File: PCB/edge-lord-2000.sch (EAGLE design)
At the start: 40 parts, among them Q1 SI2302CDS, Q2 SI2302CDS, Q3 SI2302CDS, Q4 SI2302CDS, Q5 ON Semi NTS4173P, Q6 2N7002

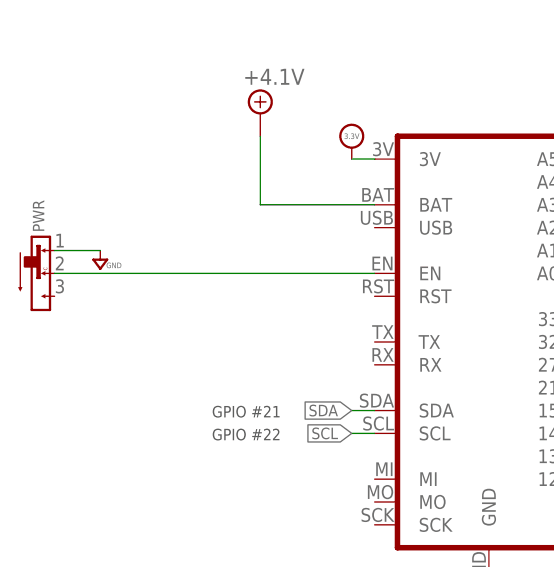
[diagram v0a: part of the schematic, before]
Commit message: PWR switch was backward. Updated 3D model for fusion.
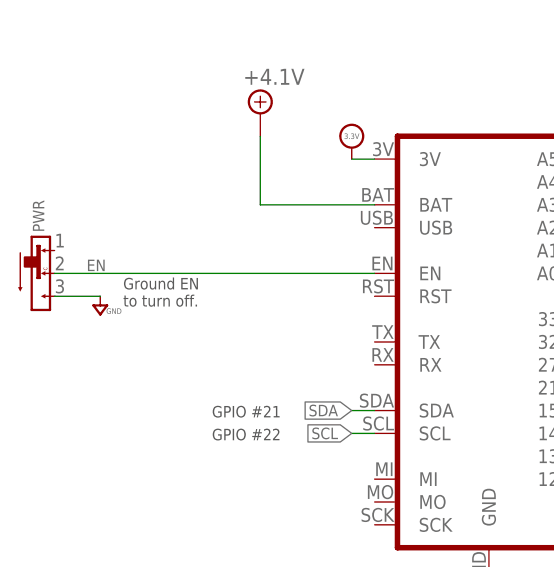
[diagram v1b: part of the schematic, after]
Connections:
- net N$1 renamed EN
- net GND: now also PWR.3; no longer PWR.1
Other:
- note added: "Ground EN to turn off."
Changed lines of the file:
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@@
 <text x="45.466" y="105.918" size="1.27" layer="97" align="bottom-right">GPIO #22</text>
 <text x="45.466" y="108.458" size="1.27" layer="97" align="bottom-right">GPIO #21</text>
+<text x="27.94" y="123.952" size="1.27" layer="97" align="top-left">Ground EN
+to turn off.</text>
 </plain>
 <instances>
@@
 </instance>
 <instance part="HUZZAH" gate="G$1" x="68.58" y="109.22" smashed="yes"/>
-<instance part="SUPPLY1" gate="GND" x="25.4" y="127" smashed="yes">
-<attribute name="VALUE" x="26.924" y="125.349" size="0.6096" layer="96" font="vector" align="center"/>
+<instance part="SUPPLY1" gate="GND" x="25.4" y="121.92" smashed="yes">
+<attribute name="VALUE" x="26.924" y="120.269" size="0.6096" layer="96" font="vector" align="center"/>
 </instance>
 <instance part="SUPPLY2" gate="GND" x="68.58" y="91.44" smashed="yes">
@@
 </busses>
 <nets>
-<net name="N$1" class="0">
+<net name="EN" class="0">
 <segment>
 <pinref part="HUZZAH" gate="G$1" pin="EN"/>
 <wire x1="55.88" y1="124.46" x2="20.32" y2="124.46" width="0.1524" layer="91"/>
 <pinref part="PWR" gate="G$1" pin="2"/>
+<label x="23.876" y="124.714" size="1.27" layer="95"/>
 </segment>
 </net>
@@
 <pinref part="HUZZAH" gate="G$1" pin="GND"/>
 <pinref part="SUPPLY2" gate="GND" pin="GND"/>
-</segment>
-<segment>
-<pinref part="SUPPLY1" gate="GND" pin="GND"/>
-<wire x1="20.32" y1="127" x2="25.4" y2="127" width="0.1524" layer="91"/>
-<pinref part="PWR" gate="G$1" pin="1"/>
 </segment>
 <segment>
@@
 <pinref part="SUPPLY35" gate="GND" pin="GND"/>
 </segment>
+<segment>
+<pinref part="PWR" gate="G$1" pin="3"/>
+<pinref part="SUPPLY1" gate="GND" pin="GND"/>
+<wire x1="20.32" y1="121.92" x2="25.4" y2="121.92" width="0.1524" layer="91"/>
+</segment>
 </net>

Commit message: PCB Rev.A tweaks.
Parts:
- R4: value XXX -> 330
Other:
- note added: "TODO: -nothing for now"
- note removed: "TODO: - P-FET needs 1N7002 on gate to work properly. - Caps accross motor load - Bulk cap for motor power. 47 -100uF - Power switch up/down reversed. - Measure motor draw when turned off. - Fuse on BAT out. - Fuse on sensor power. - Mode up/down buttons are swapped - Vibe connector TRS jack holes are enormous. Slim them down."

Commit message: Bodge Notes added to schematic
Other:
- note added: "Bodge Notes: - MOT2 and MOT3 don't work as they were routed onto INPUT only pins. Cut traces and moved to SCK(5) and MO (18) pins. But SCK has signal on it during programming. Causing motor to run. - Rev.B Move buttons to input only pins and use output pins (non-SCK) for motors."
- note added: "TODO: - change button pins to use input only pins. -change MOT3 MOT4 to use non-SCK/MO pins. - MOTORS connector channel order should be reversed, should go left to right."
- note removed: "TODO: -nothing for now"
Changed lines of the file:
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@@
 <text x="93.726" y="123.698" size="1.27" layer="97">GPIO #26</text>
 <text x="93.726" y="126.238" size="1.27" layer="97">GPIO #25</text>
-<text x="55.88" y="185.42" size="5.08" layer="97">TODO:
--nothing for now</text>
+<text x="7.62" y="53.34" size="2.54" layer="97">TODO:
+- change button pins to use input only pins.
+-change MOT3 MOT4 to use non-SCK/MO pins.
+- MOTORS connector channel order should
+  be reversed, should go left to right.</text>
 <text x="94.996" y="134.112" size="1.27" layer="97">GPIO #15</text>
 <text x="45.466" y="105.918" size="1.27" layer="97" align="bottom-right">GPIO #22</text>
@@
 <text x="27.94" y="123.952" size="1.27" layer="97" align="top-left">Ground EN
 to turn off.</text>
+<text x="5.08" y="17.78" size="2.54" layer="97">Bodge Notes:
+ - MOT2 and  MOT3 don't work as they were routed
+    onto INPUT only pins.  Cut traces and moved to
+    SCK(5) and MO (18) pins.  But SCK has signal on it during programming. Causing motor to run.
+ - Rev.B Move buttons to input only pins and use output pins (non-SCK) for motors.</text>
 </plain>
 <instances>
 <instance part="FRAME1" gate="G$1" x="0" y="0" smashed="yes">
-<attribute name="DOCUMENT_NUMBER" x="0" y="0" size="1.27" layer="96"/>
+<attribute name="DOCUMENT_NUMBER" x="10.16" y="5.08" size="1.27" layer="96" display="off"/>
 </instance>
 <instance part="FRAME1" gate="G$2" x="147.32" y="0" smashed="yes">

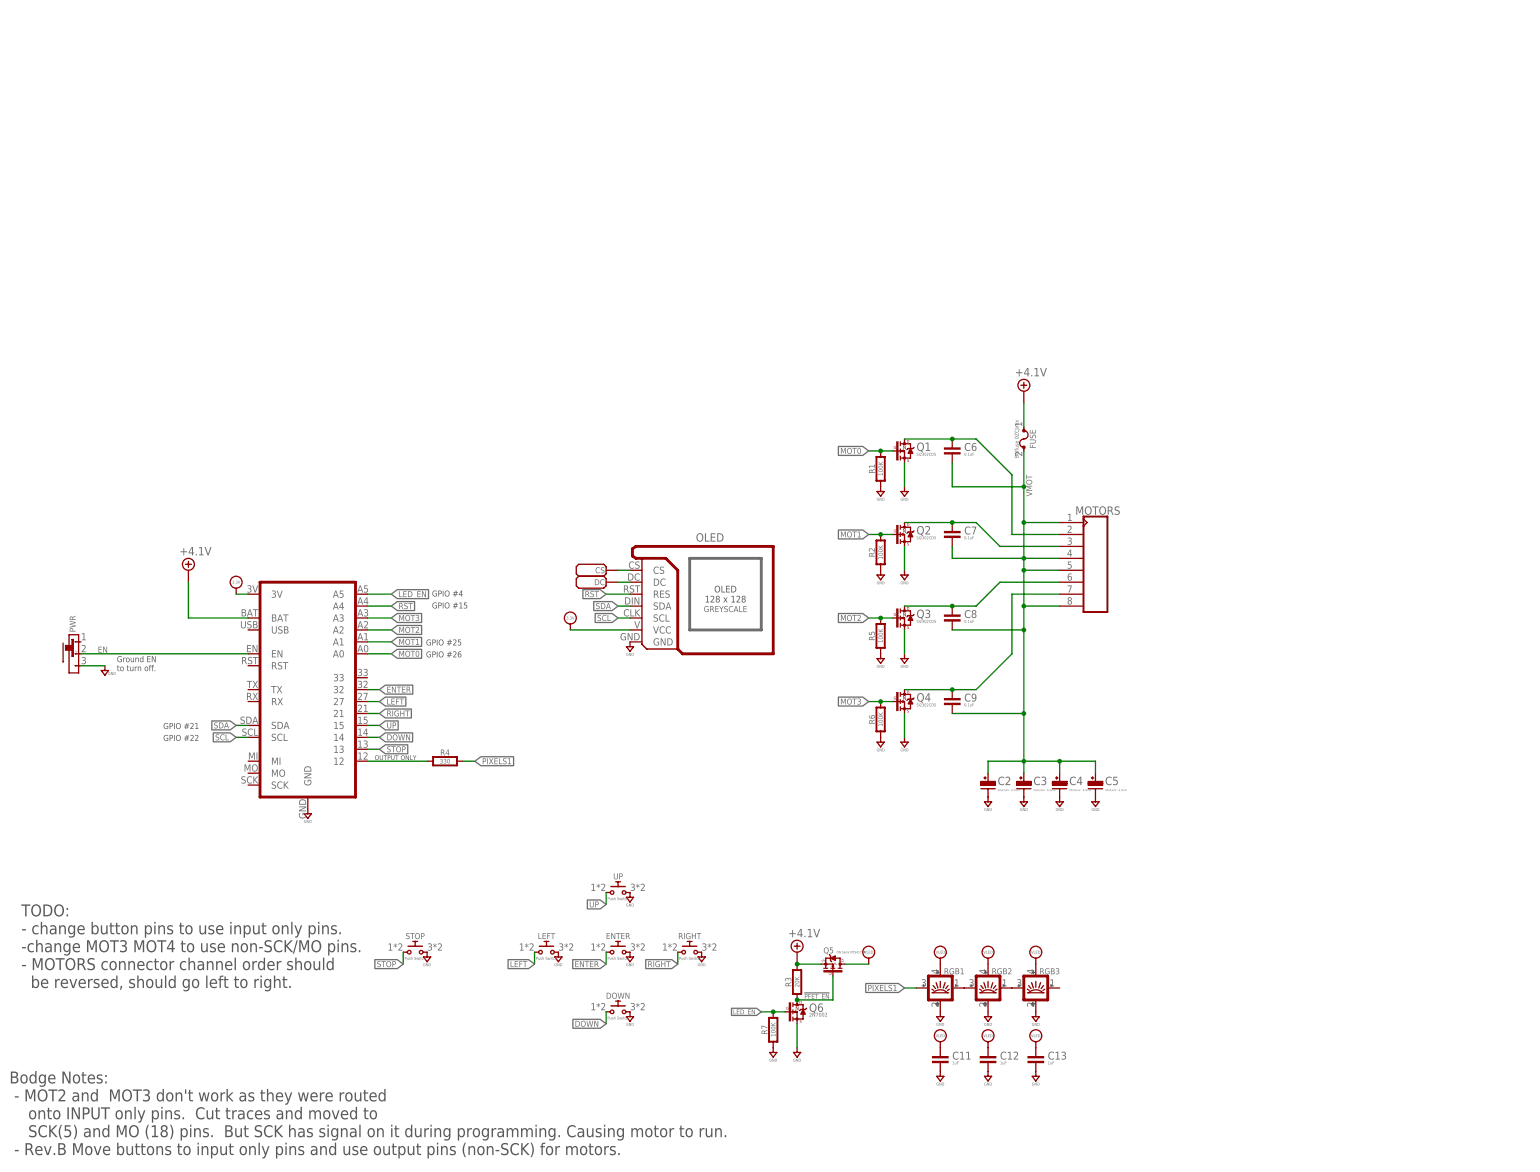
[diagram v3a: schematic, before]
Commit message: More notes in PCB. Update Huzzah symbol.
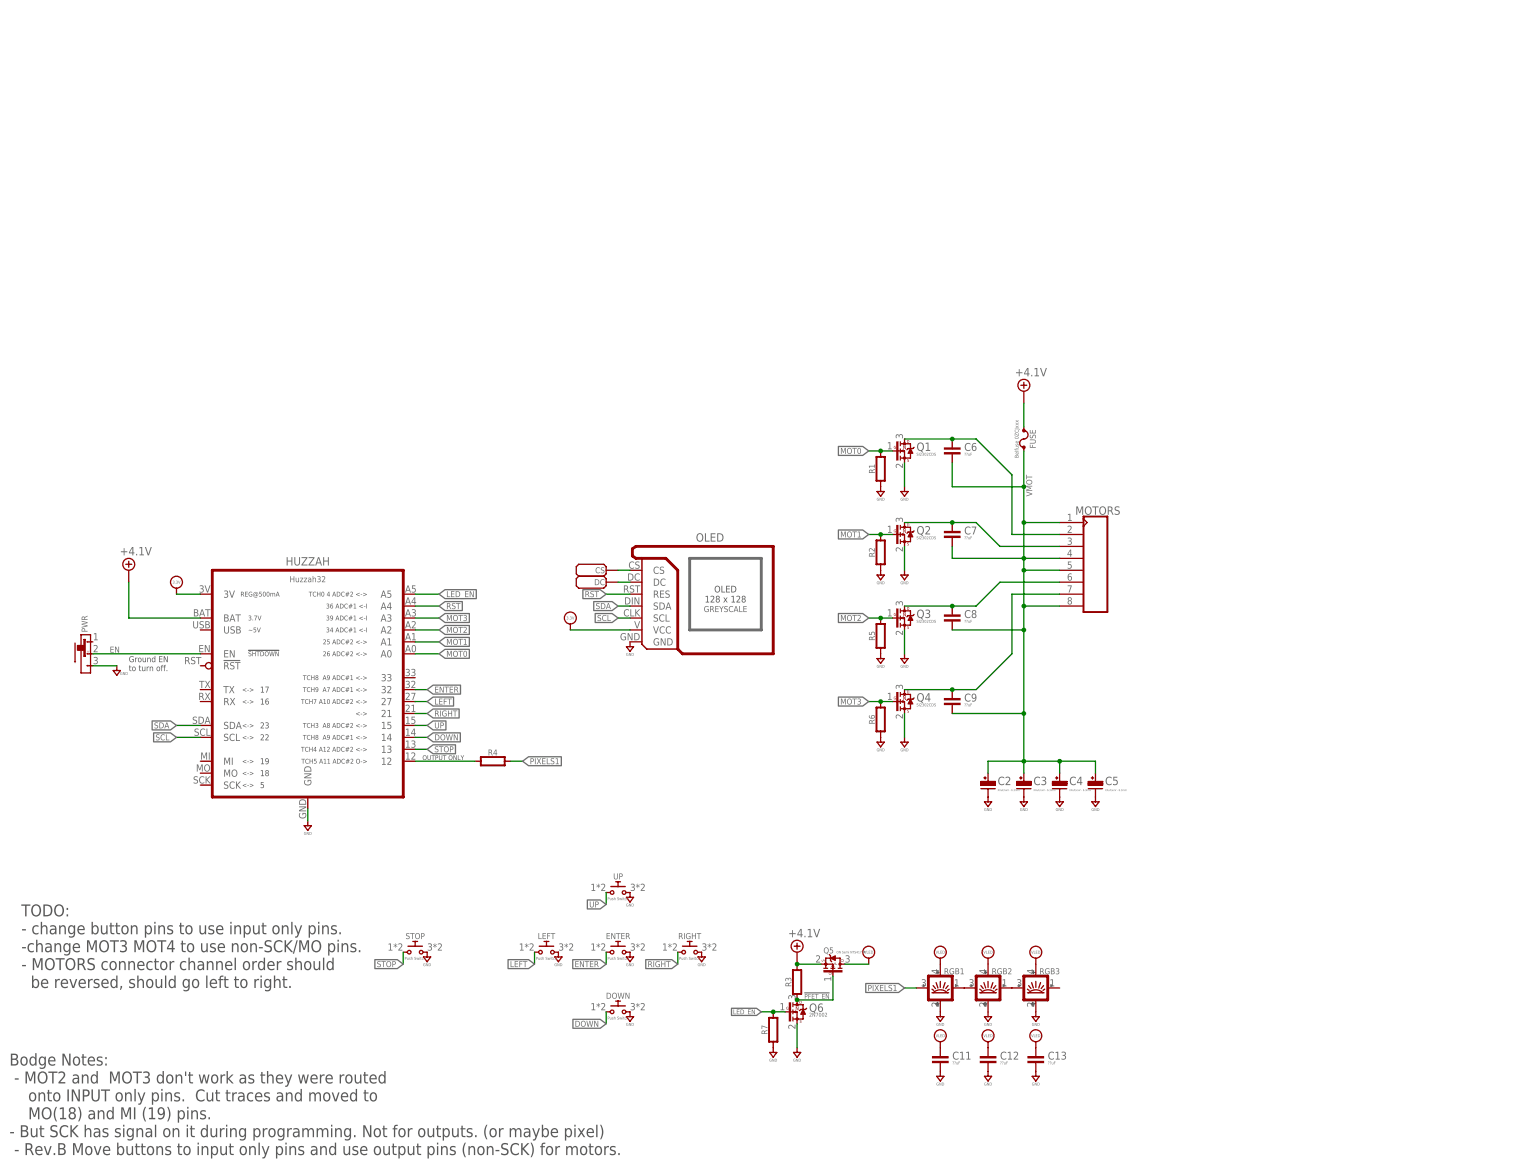
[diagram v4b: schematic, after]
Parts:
- C11, C12, C13: value 1uF -> ??uF
- C6, C7, C8, C9: value 0.1uF -> ??uF
- HUZZAH: value (none) -> Huzzah32
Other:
- note added: "Bodge Notes: - MOT2 and MOT3 don't work as they were routed onto INPUT only pins. Cut traces and moved to MO(18) and MI (19) pins. - But SCK has signal on it during programming. Not for outputs. (or maybe pixel) - Rev.B Move buttons to input only pins and use output pins (non-SCK) for motors."
- note removed: "Bodge Notes: - MOT2 and MOT3 don't work as they were routed onto INPUT only pins. Cut traces and moved to SCK(5) and MO (18) pins. But SCK has signal on it during programming. Causing motor to run. - Rev.B Move buttons to input only pins and use output pins (non-SCK) for motors."
- note removed: "GPIO #15"
- note removed: "GPIO #21"
- note removed: "GPIO #22"
- note removed: "GPIO #25"
- note removed: "GPIO #26"
- note removed: "GPIO #4"
- moved on the sheet: PWR, R4
